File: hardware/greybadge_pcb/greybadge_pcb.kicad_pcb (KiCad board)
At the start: 2 copper layers, 75 x 99 mm, 149 parts, among them J1 Conn_02x05_Row_Letter_First, J2 Conn_02x05_Row_Letter_First, J3 Conn_02x05_Row_Letter_First, J4 Conn_02x05_Row_Letter_First, J5 USB_C_Receptacle_USB2.0, Q1 Q_NMOS_GSD, SW1 SW_Push, SW2 SW_Push, SW3 SW_Push, SW4 SW_Push, SW5 SW_Push, SW6 SW_Push, SW7 SW_Push, SW8 SW_Push, SW9 SW_Push, U1 TLV62568DBV, U2 TLV62568DBV, U3 TLV73325PDBV, U4 W25Q128JVS, U5 RP2350_60QFN, U7 ECP5U_25_CABGA256, U8 W25Q128JVSIM, X1 SiT2001B, Y1 12Mhz

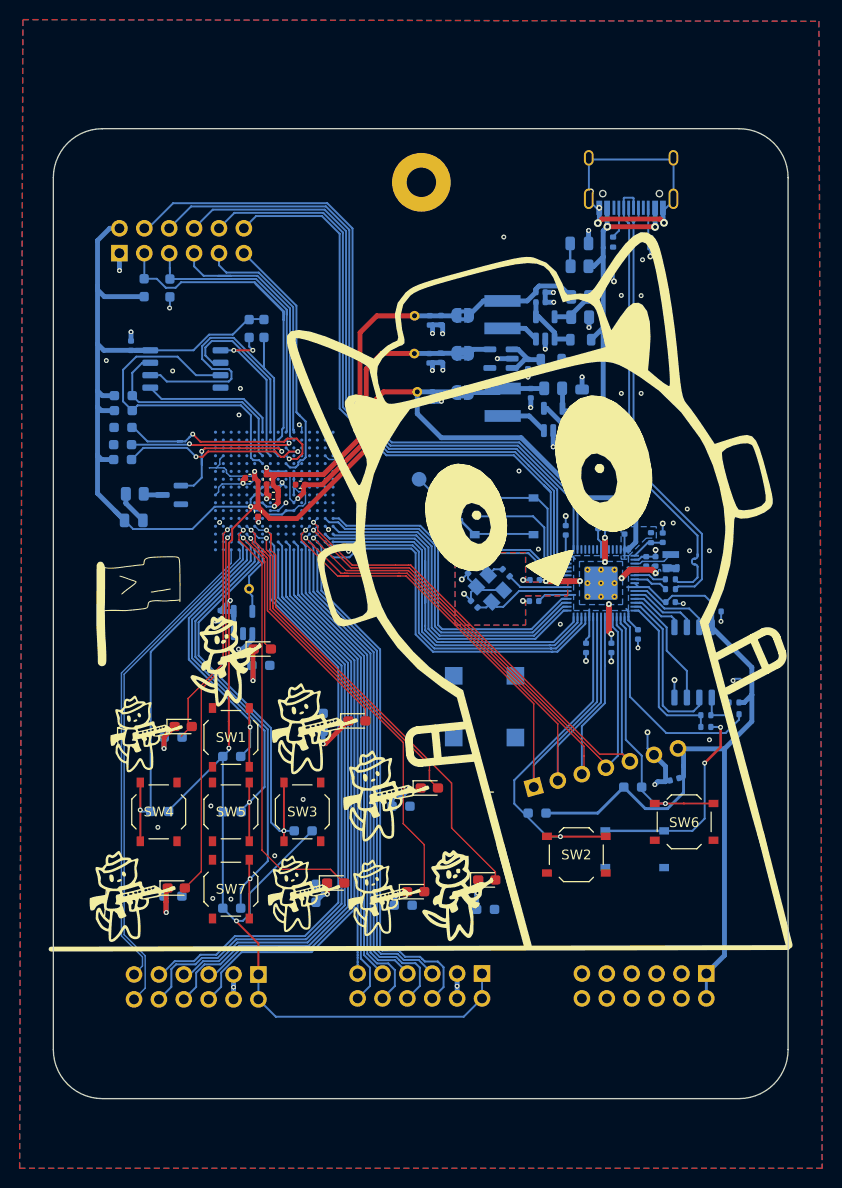
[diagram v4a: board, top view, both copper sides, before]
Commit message: feat: add lipo support
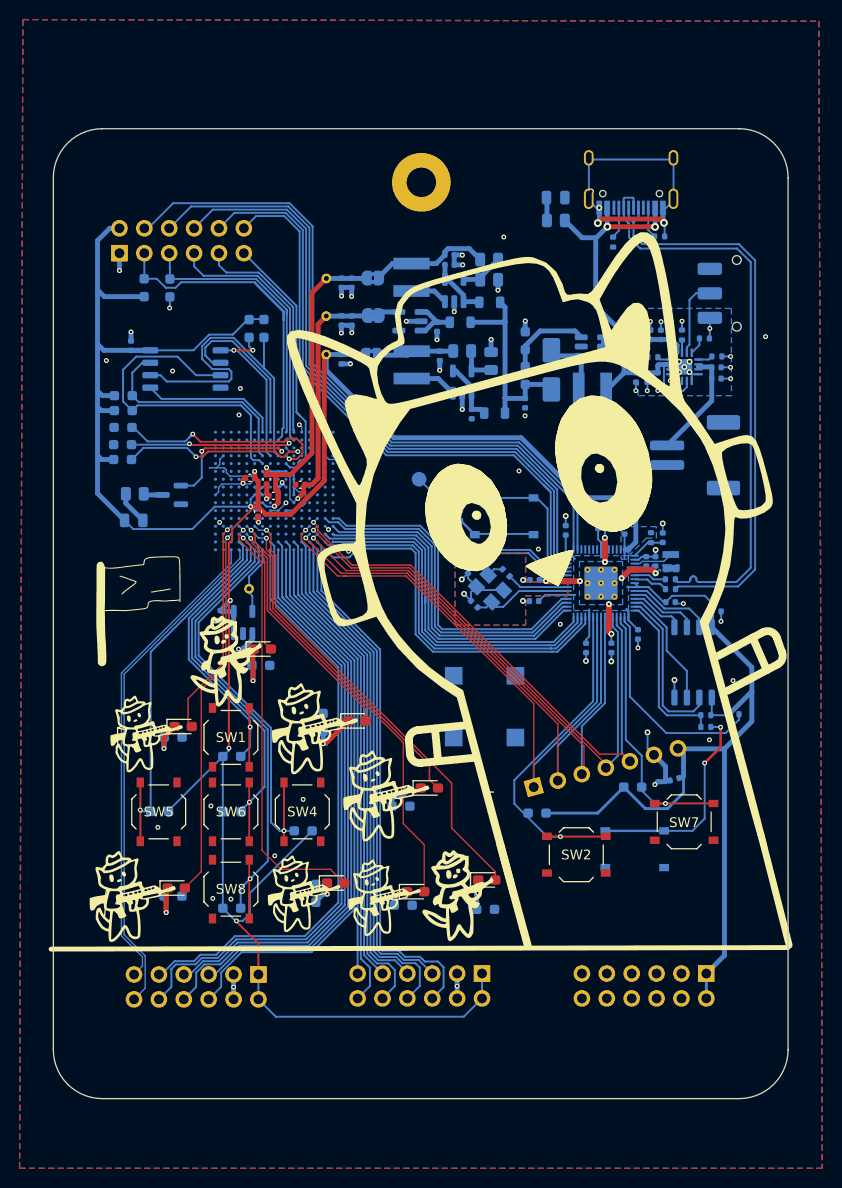
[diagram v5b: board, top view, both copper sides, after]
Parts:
- removed the C15 at (130.2, 75.0)
- removed the C16 at (120.1, 74.4)
- removed the D9 at (135.4, 62.7)
- removed the R18 at (135.5, 70.2)
- removed the R19 at (132.8, 77.5)
- removed the R20 at (135.7, 78.5)
- removed the R21 at (151.2, 109.5)
- added C10: 4.7u, Capacitor_SMD:C_0402_1005Metric, B.Cu at (122.2, 64.9)
- added C12: 4.7u, Capacitor_SMD:C_0402_1005Metric, B.Cu at (124.5, 80.1)
- added C13: 10u, Capacitor_SMD:C_0402_1005Metric, B.Cu at (121.2, 74.2)
- added C17: 10u, Capacitor_SMD:C_0402_1005Metric, B.Cu at (112.2, 66.7)
- added C20: 10u, Capacitor_SMD:C_0402_1005Metric, B.Cu at (111.2, 74.5)
- added C23: 10u, Capacitor_SMD:C_0402_1005Metric, B.Cu at (112.2, 70.6)
- added C24: 1u, Capacitor_SMD:C_0402_1005Metric, B.Cu at (120.9, 71.2)
- added C25: 1u, Capacitor_SMD:C_0402_1005Metric, B.Cu at (111.2, 70.6)
- added C6: 4u7, Capacitor_SMD:C_0402_1005Metric, B.Cu at (142.4, 76.4)
- added C7: 1u, Capacitor_SMD:C_0402_1005Metric, B.Cu at (143.5, 76.4)
- added C9: 1u, Capacitor_SMD:C_0402_1005Metric, B.Cu at (149.4, 75.3)
- added D1: SS14, Diode_SMD:D_SMA, B.Cu at (132.6, 75.6)
- added D10: LED, LED_SMD:LED_0805_2012Metric, B.Cu at (133.0, 58.0)
- added J5: 78171-0002, Connector_JST:JST_PH_S2B-PH-SM4-TB_1x02-1MP_P2.00mm_Horizontal, B.Cu at (147.2, 84.3)
- added L3: 2.2uH, Inductor_SMD:L_Taiyo-Yuden_NR-40xx, B.Cu at (118.3, 75.1)
- added R1: 200k, Resistor_SMD:R_0603_1608Metric_Pad0.98x0.95mm_HandSolder, B.Cu at (129.9, 76.2)
- added R13: 10k, Resistor_SMD:R_0402_1005Metric, B.Cu at (149.5, 74.2)
- added R15: 47k, Resistor_SMD:R_0402_1005Metric, B.Cu at (145.9, 72.0)
- added R2: 27k, Resistor_SMD:R_0603_1608Metric_Pad0.98x0.95mm_HandSolder, B.Cu at (129.9, 72.6)
- added R22: 100k, Resistor_SMD:R_0805_2012Metric, B.Cu at (126.2, 64.3)
- added R23: 1k, Resistor_SMD:R_0805_2012Metric, B.Cu at (133.0, 60.4)
- added R24: 120k, Resistor_SMD:R_0805_2012Metric, B.Cu at (126.2, 66.4)
- added R25: 68k, Resistor_SMD:R_0805_2012Metric, B.Cu at (123.5, 73.7)
- added R26: 15k, Resistor_SMD:R_0805_2012Metric, B.Cu at (126.4, 74.7)
- added SW3: SW_SPDT, Button_Switch_SMD:SW_SPDT_CK_JS102011SAQN, B.Cu at (151.5, 67.8)
- added U4: TLV62568DBV, Package_TO_SOT_SMD:SOT-23-5, B.Cu at (123.5, 76.8)
- added U5: TLV73325PDBV, Package_TO_SOT_SMD:SOT-23-5, B.Cu at (118.2, 70.6)
- C1: value 4.7u -> 22u
- C11: value 10u -> 22u
- C14: value 10u -> 100n
- C3: value 4.7u -> 4u7
- C4, C8: value 10u -> 4u7
- C5: value 100n -> 1u
- L1: value 2.2uH -> 22uH
- R16: value 100k -> 1k5; footprint Resistor_SMD:R_0805_2012Metric -> Resistor_SMD:R_0402_1005Metric
- R17: value 1k -> 2k2; footprint Resistor_SMD:R_0805_2012Metric -> Resistor_SMD:R_0402_1005Metric
- U1: value TLV62568DBV -> MT3608; footprint Package_TO_SOT_SMD:SOT-23-5 -> Package_TO_SOT_SMD:SOT-23-6
- U2: value TLV62568DBV -> BQ24075; footprint Package_TO_SOT_SMD:SOT-23-5 -> Package_DFN_QFN:VQFN-16-1EP_3x3mm_P0.5mm_EP1.6x1.6mm
- U3: value TLV73325PDBV -> TLV62568DBV
- moved C8 28.7 mm to (149.4, 76.5), turned to 0 degrees
- moved C5 24.7 mm to (144.8, 72.0), turned to 90 degrees
- moved L2 15.8 mm to (118.3, 66.2)
- moved R17 14.7 mm to (148.2, 72.4)
- moved C11 14.6 mm to (122.2, 63.9), turned to 0 degrees
- moved U2 14.4 mm to (146.2, 75.3), turned to 180 degrees
- moved C4 13.6 mm to (142.7, 72.0), turned to 90 degrees
- moved C3 13.5 mm to (143.8, 72.0), turned to 90 degrees
- moved C2 13.1 mm to (141.2, 76.4), turned to -90 degrees
- moved C14 12.7 mm to (111.2, 66.7)
- moved L1 12.0 mm to (136.8, 77.7), turned to 180 degrees
- moved FB2 11.1 mm to (126.8, 80.0)
- moved C1 10.4 mm to (129.9, 79.0), turned to -90 degrees
- moved FB3 10.0 mm to (123.3, 70.7)
- moved JP2 10.0 mm to (114.2, 74.1)
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- renumbered C6 to C15, C7 to C16, C9 to C18, C10 to C19, C35 to C21, C12 to C22, C17 to C26, C18 to C27, C19 to C28, C20 to C29, C21 to C30, C22 to C31, C23 to C32, C24 to C33, C25 to C34, C26 to C35, C27 to C36, C28 to C37, C29 to C38, C30 to C39, C31 to C40, C32 to C41, C36 to C42, C37 to C43, D10 to D11, D1 to D2, D2 to D3, D3 to D4, D4 to D5, D5 to D6, D6 to D7, D7 to D8, D8 to D9, J4 to J1, J1 to J2, J2 to J3, J3 to J4, J5 to J6, L3 to L4, R8 to R10, R9 to R11, R10 to R12, R11 to R14, R12 to R18, R13 to R19, R14 to R20, R15 to R21, R22 to R27, R23 to R28, R24 to R29, R1 to R3, R25 to R30, R26 to R31, R27 to R32, R28 to R33, R29 to R34, R30 to R35, R31 to R36, R32 to R37, R33 to R38, R34 to R39, R2 to R4, R35 to R40, R36 to R41, R37 to R42, R38 to R43, R39 to R44, R40 to R45, R41 to R46, R3 to R5, R4 to R6, R5 to R7, R6 to R8, R7 to R9, SW9 to SW10, SW3 to SW4, SW4 to SW5, SW5 to SW6, SW6 to SW7, SW7 to SW8, SW8 to SW9, U4 to U6, U5 to U7, U7 to U8, U8 to U9
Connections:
- C1 pad 1: Net-(U1-EN) -> +5V
- C11 pad 1: +3V3 -> Net-(JP1-A)
- C14 pad 1: +F2V5 -> +F1V1
- C2 pad 1: Net-(JP1-A) -> +BQ_OUT
- C3 pad 1: Net-(U2-EN) -> +5V_USB
- C4 pad 1: Net-(JP2-A) -> +5V_USB
- C5 pad 1: +F1V1 -> +5V_USB
- C8 pad 1: +F1V1 -> +BATT
- FB1 pad 1: Net-(U1-EN) -> Net-(U3-EN)
- FB2 pad 1: Net-(U2-EN) -> Net-(U4-EN)
- FB3 pad 1: Net-(U3-EN) -> Net-(U5-EN)
- J6 pad A4: +5V -> +5V_USB
- J6 pad A9: +5V -> +5V_USB
- J6 pad B4: +5V -> +5V_USB
- J6 pad B9: +5V -> +5V_USB
- L1 pad 1: Net-(U1-SW) -> +BQ_OUT
- L1 pad 2: Net-(JP1-A) -> Net-(D1-A)
- L2 pad 1: Net-(U2-SW) -> Net-(U3-SW)
- L2 pad 2: Net-(JP2-A) -> Net-(JP1-A)
- R16 pad 1: Net-(U1-FB) -> /ILIM
- R16 pad 2: Net-(JP1-A) -> GND
- R17 pad 1: Net-(D9-A) -> Net-(U2-ISET)
- R17 pad 2: +5V -> GND
- U1 pad 1: Net-(U1-EN) -> Net-(D1-A)
- U1 pad 3: Net-(U1-SW) -> Net-(U1-FB)
- U1 pad 4: Net-(U1-EN) -> +BQ_OUT
- U1 pad 5: Net-(U1-FB) -> +BQ_OUT
- U2 pad 1: Net-(U2-EN) -> Net-(U2-TS)
- U2 pad 2: GND -> +BATT
- U2 pad 3: Net-(U2-SW) -> +BATT
- U2 pad 4: Net-(U2-EN) -> GND
- U2 pad 5: Net-(U2-FB) -> GND
- U3 pad 3: Net-(U3-EN) -> Net-(U3-SW)
- U3 pad 4: unconnected-(U3-NC-Pad4) -> Net-(U3-EN)
- U3 pad 5: +F2V5 -> Net-(U3-FB)
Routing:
- net +5V_USB: track 0.00 -> 31.6 mm, vias 0 -> 2
- net +BQ_OUT: track 0.00 -> 19.0 mm
- net +5V: track 39.1 -> 21.4 mm, vias 2 -> 0
- net mcu_swd: track 34.3 -> 20.6 mm
- net /rp2350/USB_D+: track 45.5 -> 58.4 mm
- net /rp2350/USB_D-: track 47.1 -> 59.9 mm
- net +BATT: track 0.00 -> 12.8 mm
- net GND: track 119.2 -> 131.9 mm, vias 88 -> 91
- net +3V3: track 370.6 -> 381.5 mm
- net Net-(SW3-B): track 0.00 -> 7.86 mm
- net Net-(D1-A): track 0.00 -> 6.95 mm
- net Net-(U1-EN): track 6.35 -> 0.00 mm
- net Net-(U4-EN): track 0.00 -> 6.32 mm
- net Net-(U2-EN): track 6.11 -> 0.00 mm
- net Net-(U5-EN): track 0.00 -> 5.34 mm
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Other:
- board text added: "100n"
- board text added: "4.7u"
- board text added: "C23"
- board text added: "R26"
- board text added: "R30"
- board text added: "R31"

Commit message: feat: Add pads for AA batt
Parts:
- added AA+1: TestPoint, TestPoint:TestPoint_Pad_D1.5mm, B.Cu at (139.0, 83.4)
- added AA-1: TestPoint, TestPoint:TestPoint_Pad_D1.5mm, B.Cu at (135.5, 83.4)
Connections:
- net +BQ_OUT renamed +AA_OUT
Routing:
- net +AA_OUT: track 19.0 -> 25.1 mm
- net GND: track 131.9 -> 135.8 mm, vias 91 -> 93
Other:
- board text added: "AA+"
- board text added: "AA-"
